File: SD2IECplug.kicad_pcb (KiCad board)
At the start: 2 copper layers, 48 x 88 mm, 57 parts, among them J1 ISP, J2 LED/SW, J3 SD_Card, J4 IEC, J5 C64-CassettePort, J6 C64-CassettePort, J7 USB_B, Q1 IRLML2803, Q2 IRLML2803, Q3 IRLML2803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

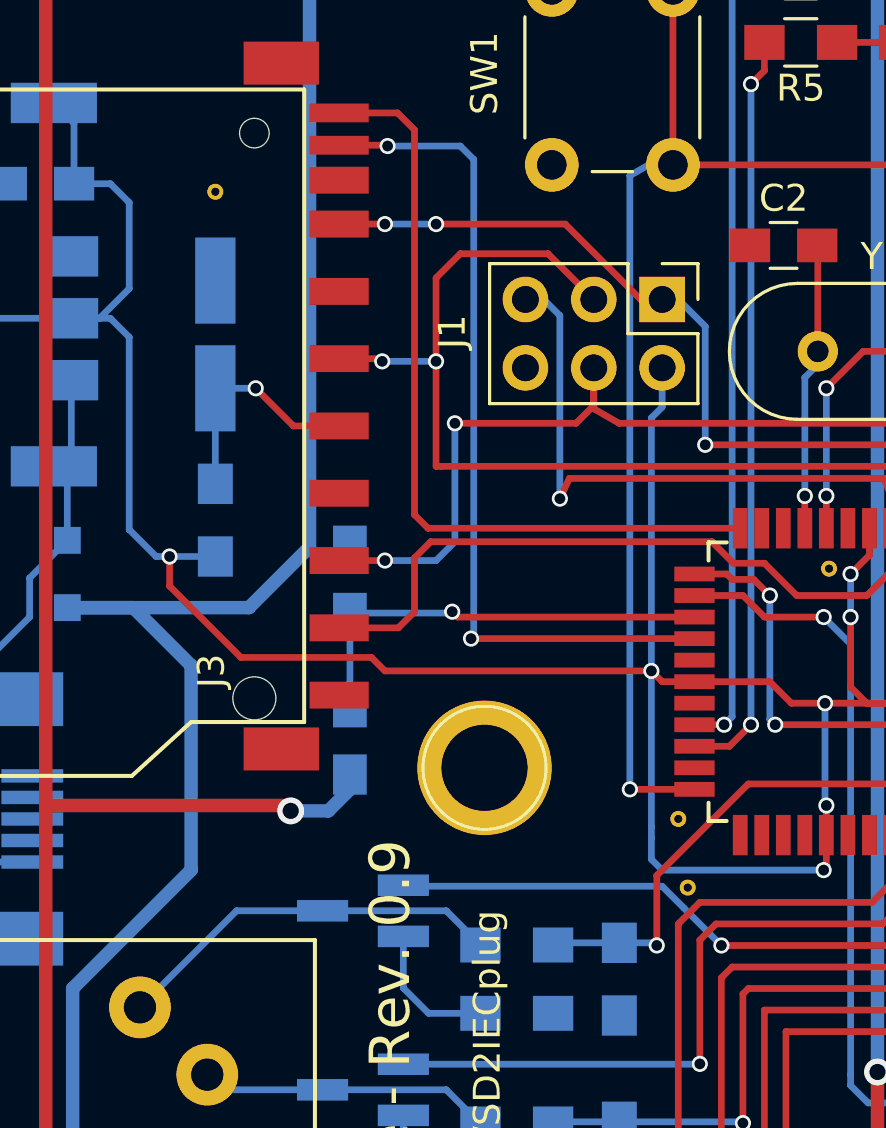
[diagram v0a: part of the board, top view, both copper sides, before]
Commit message: Added optional I2C connector.
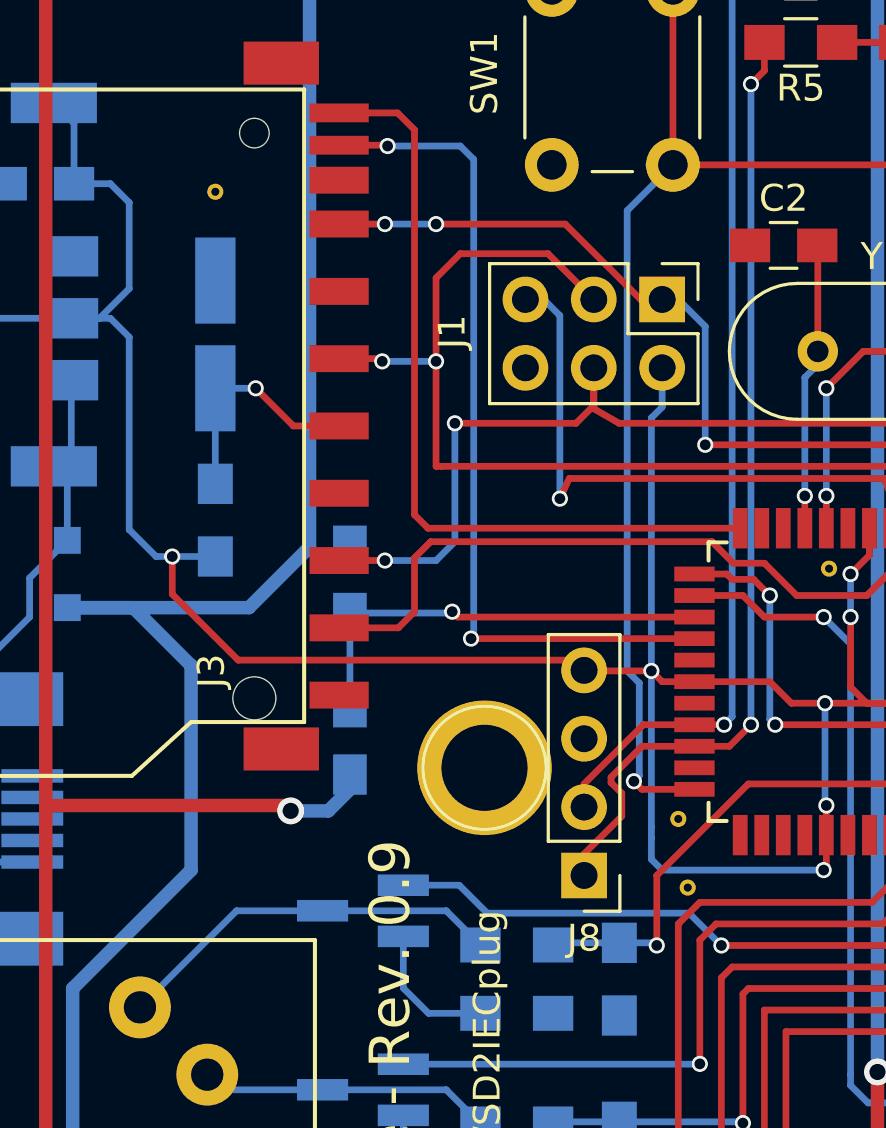
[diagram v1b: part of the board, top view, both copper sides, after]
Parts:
- added J8: I2C, Pin_Headers:Pin_Header_Straight_1x04_Pitch2.54mm, F.Cu at (85.7, 102.2)
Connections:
- net Net-(R1-Pad2) renamed SCL
- net Net-(R5-Pad2) renamed SDA
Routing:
- net SDA: track 28.0 -> 36.0 mm
- net SCL: track 30.2 -> 36.1 mm

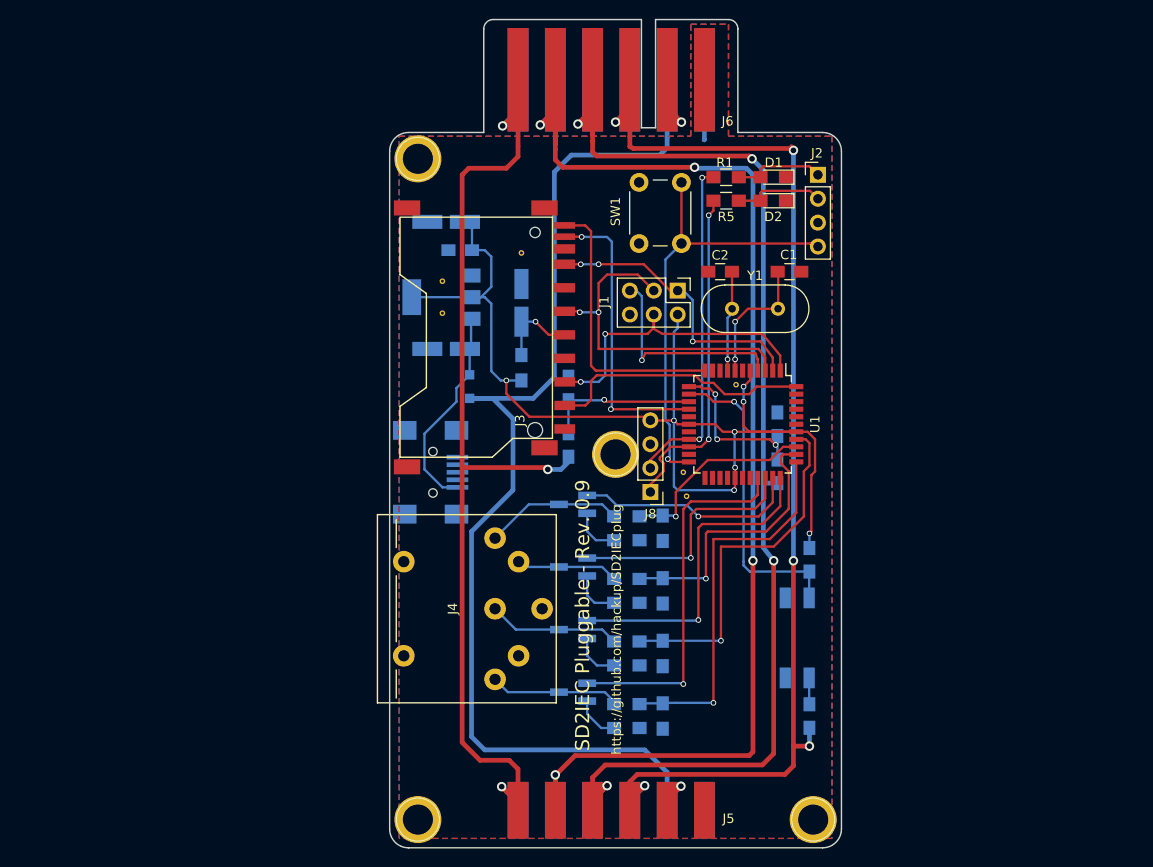
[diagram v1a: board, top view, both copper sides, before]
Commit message: Removed push button, added switch header.
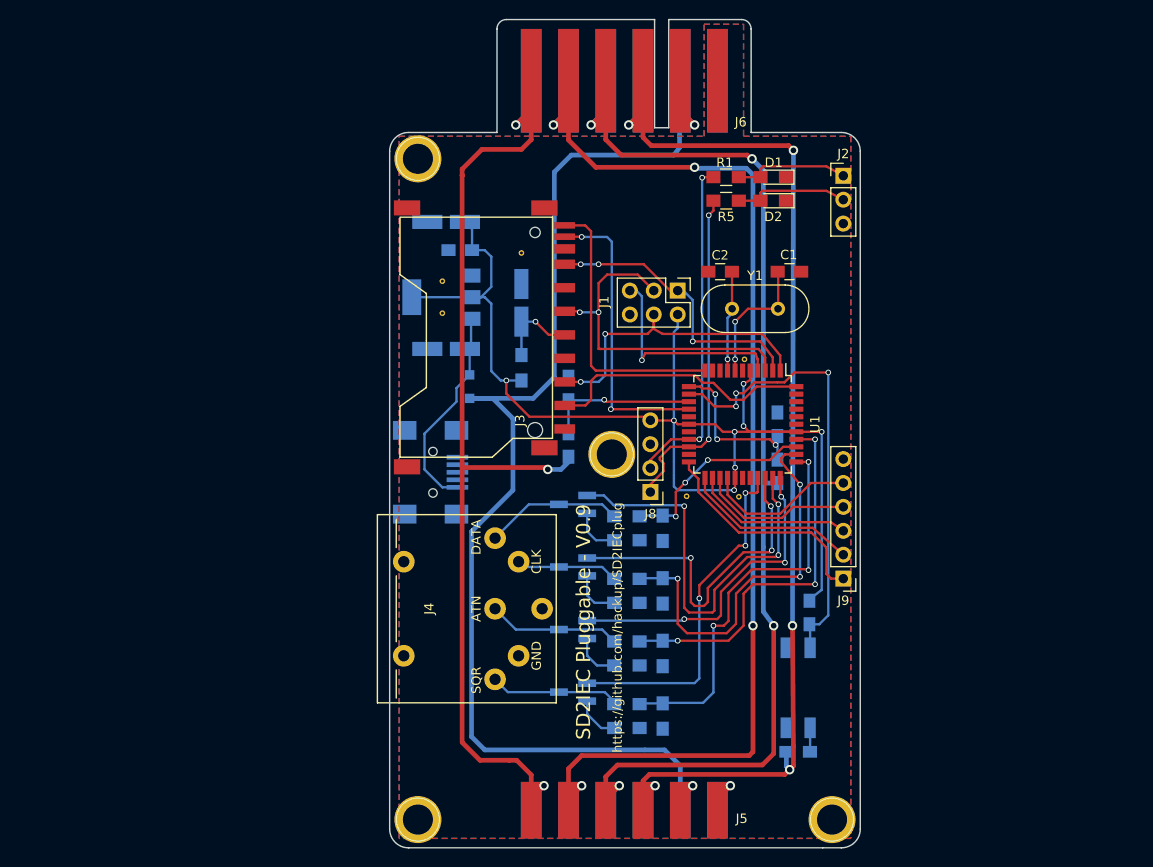
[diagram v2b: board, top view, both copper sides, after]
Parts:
- removed SW1: DiskSwitch, Buttons_Switches_THT:SW_PUSH_6mm
- added J9: SW, Pin_Headers:Pin_Header_Straight_1x06_Pitch2.54mm, F.Cu at (106.2, 111.4)
- J2: value LED/SW -> LED; footprint Pin_Headers:Pin_Header_Straight_1x04_Pitch2.54mm -> Pin_Headers:Pin_Header_Straight_1x03_Pitch2.54mm
- moved REF** 6.45 mm to (95.1, 102.7)
- moved R21 5.60 mm to (102.6, 115.0)
- moved U3 5.30 mm to (101.4, 123.0)
- moved R20 3.98 mm to (101.4, 129.8), turned to 180 degrees
- moved REF** 2.85 mm to (95.7, 88.1)
- moved J2 2.70 mm to (106.2, 68.6)
- moved REF** 2.00 mm to (105.0, 137.0)
- moved J6 1.40 mm to (82.4, 64.0)
- moved J5 1.40 mm to (82.4, 139.0)
- moved REF** 0.40 mm to (81.6, 98.2)
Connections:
- U1 pad 22: Net-(J2-Pad4) -> Net-(J9-Pad1)
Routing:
- net Net-(J2-Pad4): track 48.2 -> 0.00 mm, vias 1 -> 0
- net Net-(J9-Pad1): track 0.00 -> 24.5 mm
- net Net-(Q2-Pad1): track 23.9 -> 44.1 mm, vias 1 -> 3
- net Net-(J9-Pad2): track 0.00 -> 18.9 mm
- net Net-(J9-Pad3): track 0.00 -> 17.1 mm
- net Net-(J9-Pad4): track 0.00 -> 16.3 mm
- net Net-(J9-Pad5): track 0.00 -> 16.3 mm
- net Net-(R21-Pad2): track 33.0 -> 48.4 mm, vias 1 -> 3
- net Net-(R10-Pad2): track 29.4 -> 41.8 mm, vias 1 -> 3
- net Cas-Write: track 142.5 -> 130.6 mm
- net Cas-Read: track 137.5 -> 127.7 mm
- net Net-(Q3-Pad1): track 26.4 -> 35.8 mm, vias 1 -> 3
- net Cas-5V: track 136.1 -> 144.1 mm
- net +3V3: track 122.4 -> 129.7 mm
- net Cas-GND: track 11.9 -> 6.33 mm, vias 0 -> 1
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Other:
- board size 48 x 88 mm -> 50 x 88 mm
- board text added: "ATN"
- board text added: "CLK"
- board text added: "DATA"
- board text added: "GND"
- board text added: "SD2IEC Pluggable - V0.9"
- board text added: "SQR"
- board text removed: "SD2IEC Pluggable - Rev. 0.9"

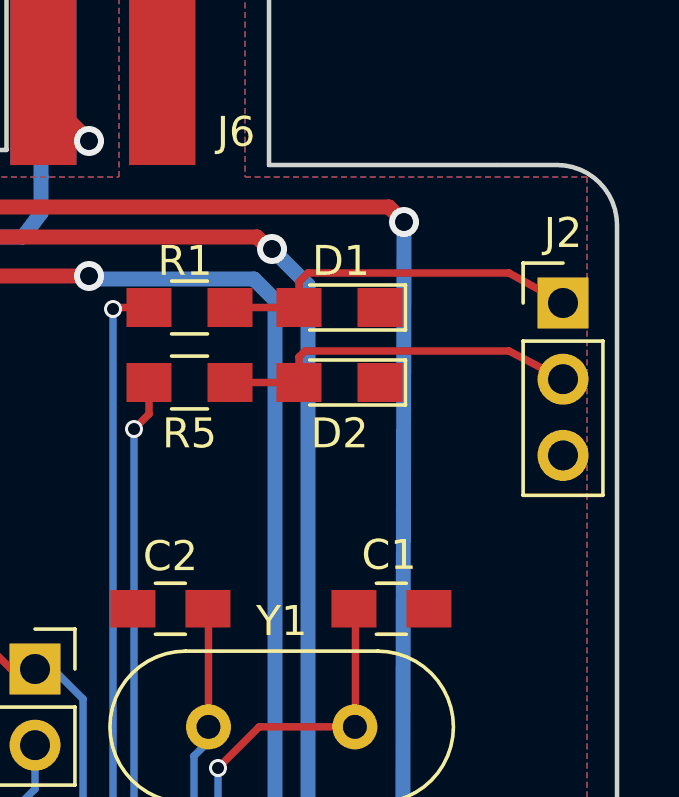
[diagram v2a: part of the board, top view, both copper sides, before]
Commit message: Added another mounting hole.
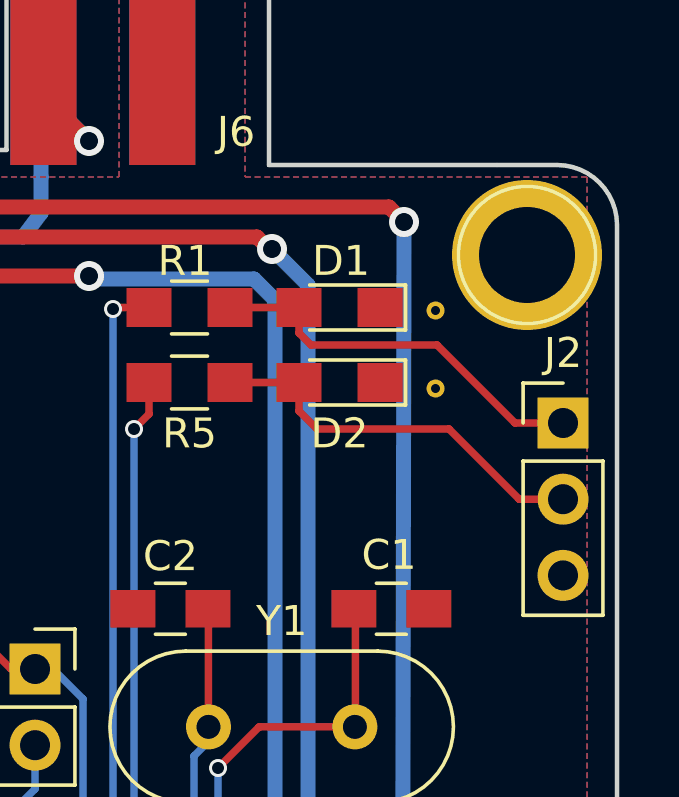
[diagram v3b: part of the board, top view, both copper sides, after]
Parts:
- added REF**: VIA-0.6mm, hackup:VIA-0.6mm, F.Cu at (102.0, 71.5)
- added REF**: VIA-0.6mm, hackup:VIA-0.6mm, F.Cu at (102.0, 68.8)
- added REF**: 1pin, Connectors:1pin, F.Cu at (105.0, 67.0)
- moved J2 4.00 mm to (106.2, 72.6)
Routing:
- net Net-(D2-Pad2): track 12.3 -> 13.3 mm
- net Net-(D1-Pad2): track 12.3 -> 13.2 mm
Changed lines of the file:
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@@
 (kicad_pcb (version 4) (host pcbnew 4.0.7)
   (general
-    (links 141)
+    (links 143)
     (no_connects 0)
     (area 57.924999 51.924999 108.075001 140.075001)
     (thickness 1.6)
     (drawings 31)
-    (tracks 567)
+    (tracks 569)
     (zones 0)
-    (modules 58)
+    (modules 61)
     (nets 61)
   )
@@
   )
   (module hackup:VIA-0.6mm (layer F.Cu)
+    (at 101.95 71.45)
+    (fp_text reference REF** (at 0 1.2) (layer F.SilkS) hide
+      (effects (font (size 1 1) (thickness 0.15)))
+    )
+    (fp_text value VIA-0.6mm (at 0 -1) (layer F.Fab) hide
+      (effects (font (size 1 1) (thickness 0.15)))
+    )
+    (pad "" thru_hole circle (at 0 0) (size 0.6 0.6) (drill 0.3) (layers *.Cu)
+      (net 41 Cas-GND) (zone_connect 2))
+  )
+  (module hackup:VIA-0.6mm (layer F.Cu)
+    (at 101.95 68.85)
+    (fp_text reference REF** (at 0 1.2) (layer F.SilkS) hide
+      (effects (font (size 1 1) (thickness 0.15)))
+    )
+    (fp_text value VIA-0.6mm (at 0 -1) (layer F.Fab) hide
+      (effects (font (size 1 1) (thickness 0.15)))
+    )
+    (pad "" thru_hole circle (at 0 0) (size 0.6 0.6) (drill 0.3) (layers *.Cu)
+      (net 41 Cas-GND) (zone_connect 2))
+  )
+  (module Connectors:1pin (layer F.Cu)
+    (at 105 67)
+    (descr "module 1 pin (ou trou mecanique de percage)")
+    (tags DEV)
+    (fp_text reference REF** (at 0 0) (layer F.SilkS) hide
+      (effects (font (size 1 1) (thickness 0.15)))
+    )
+    (fp_text value 1pin (at 0 3) (layer F.Fab)
+      (effects (font (size 1 1) (thickness 0.15)))
+    )
+    (fp_circle (center 0 0) (end 2 0.8) (layer F.Fab) (width 0.1))
+    (fp_circle (center 0 0) (end 2.6 0) (layer F.CrtYd) (width 0.05))
+    (fp_circle (center 0 0) (end 0 -2.286) (layer F.SilkS) (width 0.12))
+    (pad "" thru_hole circle (at 0 0) (size 5 5) (drill 3.2) (layers *.Cu *.Mask))
+  )
+  (module hackup:VIA-0.6mm (layer F.Cu)
     (at 95.1 102.7)
     (fp_text reference REF** (at 0 1.2) (layer F.SilkS) hide
@@
   )
   (module Pin_Headers:Pin_Header_Straight_1x03_Pitch2.54mm (layer F.Cu)
-    (at 106.2 68.6)
+    (at 106.2 72.6)
     (descr "Through hole straight pin header, 1x03, 2.54mm pitch, single row")
     (tags "Through hole pin header THT 1x03 2.54mm single row")
@@
   (segment (start 66.75 74.25) (end 66 73.5) (width 0.25) (layer B.Cu) (net 5))
   (segment (start 60.35 81.5) (end 66.65 81.5) (width 0.25) (layer B.Cu) (net 5))
-  (segment (start 97.4 68.75) (end 97.4 67.9) (width 0.25) (layer F.Cu) (net 6))
-  (segment (start 104.4 67.6) (end 106.2 68.6) (width 0.25) (layer F.Cu) (net 6) (status 20))
-  (segment (start 97.7 67.6) (end 104.4 67.6) (width 0.25) (layer F.Cu) (net 6))
-  (segment (start 97.4 67.9) (end 97.7 67.6) (width 0.25) (layer F.Cu) (net 6))
+  (segment (start 97.4 68.75) (end 97.4 69.6) (width 0.25) (layer F.Cu) (net 6))
+  (segment (start 104.6 72.6) (end 106.2 72.6) (width 0.25) (layer F.Cu) (net 6))
+  (segment (start 102 70) (end 104.6 72.6) (width 0.25) (layer F.Cu) (net 6))
+  (segment (start 97.8 70) (end 102 70) (width 0.25) (layer F.Cu) (net 6))
+  (segment (start 97.4 69.6) (end 97.8 70) (width 0.25) (layer F.Cu) (net 6))
   (segment (start 95.1 68.75) (end 97.4 68.75) (width 0.25) (layer F.Cu) (net 6))
-  (segment (start 97.4 71.25) (end 97.4 70.4) (width 0.25) (layer F.Cu) (net 7))
-  (segment (start 104.4 70.2) (end 106.2 71.14) (width 0.25) (layer F.Cu) (net 7) (status 20))
-  (segment (start 97.6 70.2) (end 104.4 70.2) (width 0.25) (layer F.Cu) (net 7))
-  (segment (start 97.4 70.4) (end 97.6 70.2) (width 0.25) (layer F.Cu) (net 7))
+  (segment (start 97.4 71.25) (end 97.4 72.2) (width 0.25) (layer F.Cu) (net 7))
+  (segment (start 104.74 75.14) (end 106.2 75.14) (width 0.25) (layer F.Cu) (net 7))
+  (segment (start 102.4 72.8) (end 104.74 75.14) (width 0.25) (layer F.Cu) (net 7))
+  (segment (start 98 72.8) (end 102.4 72.8) (width 0.25) (layer F.Cu) (net 7))
+  (segment (start 97.4 72.2) (end 98 72.8) (width 0.25) (layer F.Cu) (net 7))
   (segment (start 95.1 71.25) (end 97.4 71.25) (width 0.25) (layer F.Cu) (net 7))
   (segment (start 88.6 80.8) (end 87.8 80.8) (width 0.25) (layer F.Cu) (net 8))

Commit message: Bug fix: Mini USB GND actually seems to be on pin 5.
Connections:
- J7 pad 5: Net-(J7-Pad5) -> Cas-GND

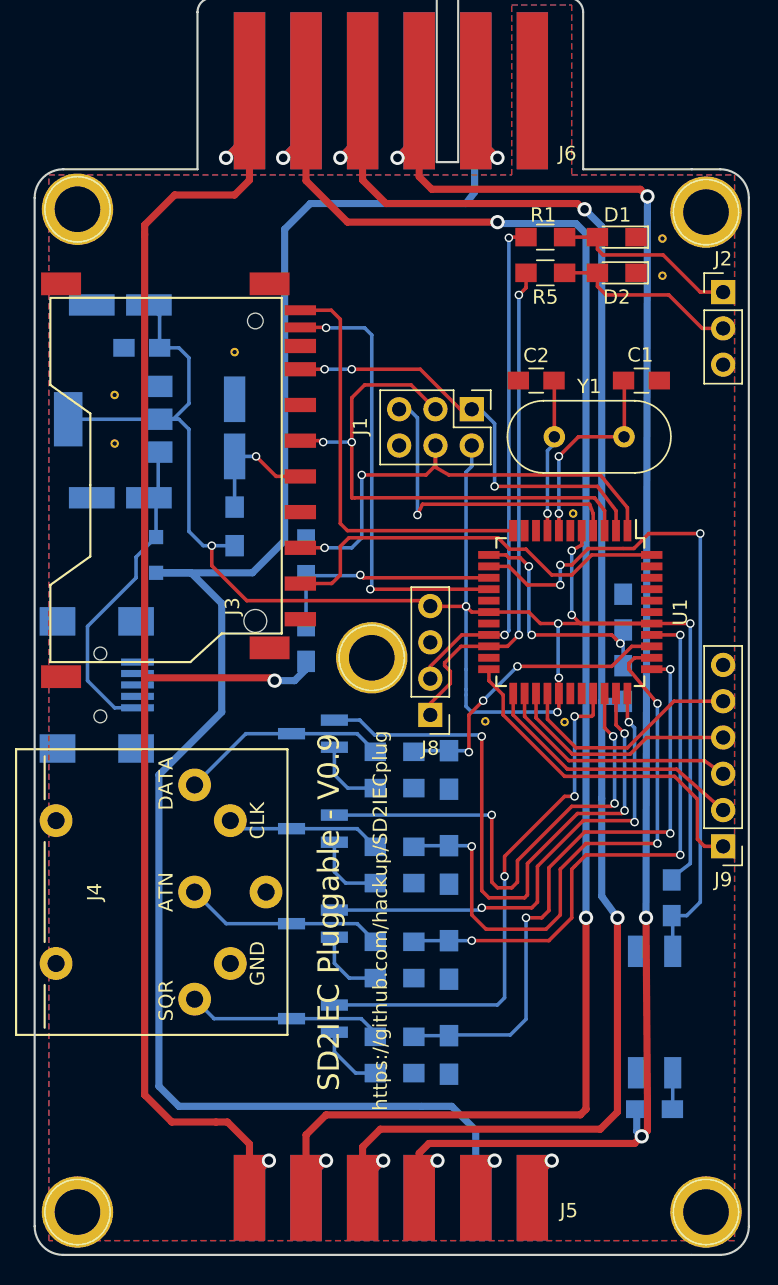
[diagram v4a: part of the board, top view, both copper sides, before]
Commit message: Changed diode D3 footprint.
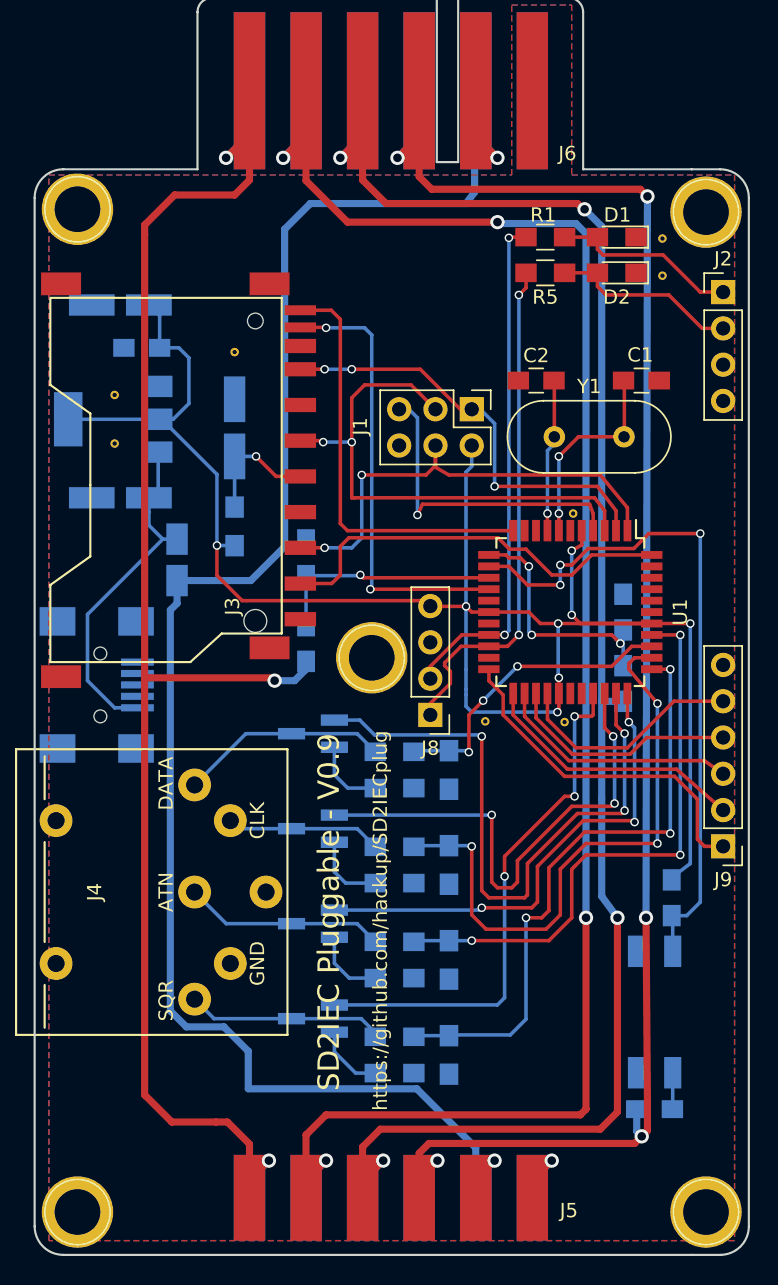
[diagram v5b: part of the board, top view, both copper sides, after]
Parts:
- D3: footprint Diodes_SMD:D_SOD-323_HandSoldering -> Diodes_SMD:D_MicroMELF_Hadsoldering
- J2: footprint Pin_Headers:Pin_Header_Straight_1x03_Pitch2.54mm -> Pin_Headers:Pin_Header_Straight_1x04_Pitch2.54mm
- moved D3 1.51 mm to (68.0, 91.3)
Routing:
- net Cas-5V: track 144.1 -> 134.6 mm
- net Net-(C4-Pad1): track 22.8 -> 26.3 mm
- net +3V3: track 129.7 -> 128.3 mm
